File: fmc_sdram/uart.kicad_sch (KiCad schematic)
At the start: 10 parts, among them J2 TYPE-C-31-M-12, U5 TPD4E02B04DQA, U6 CH343P

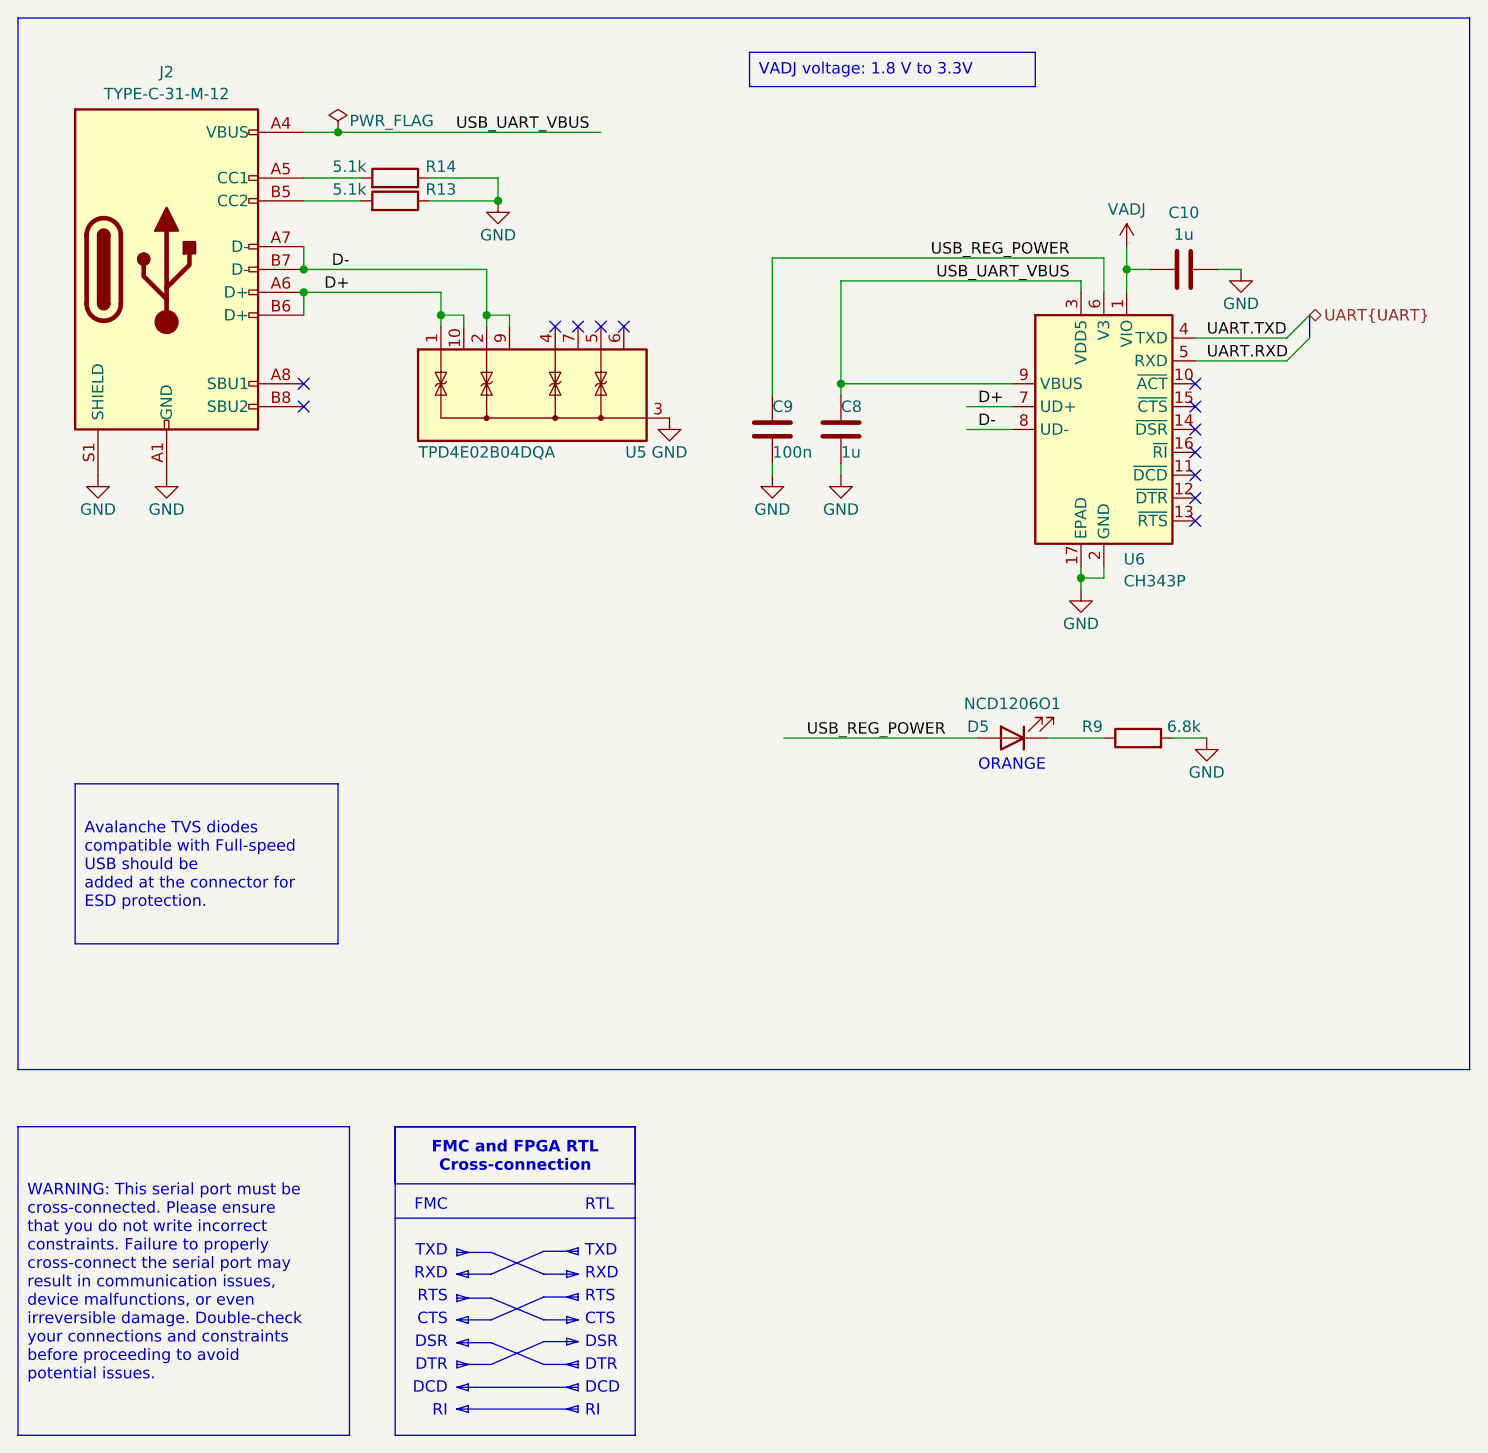
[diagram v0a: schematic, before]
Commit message: fmc_sdram: tie dqm level shifter dir pins to vadj and fix pcb
Signed-off-by: Huang Rui <vowstar@gmail.com>
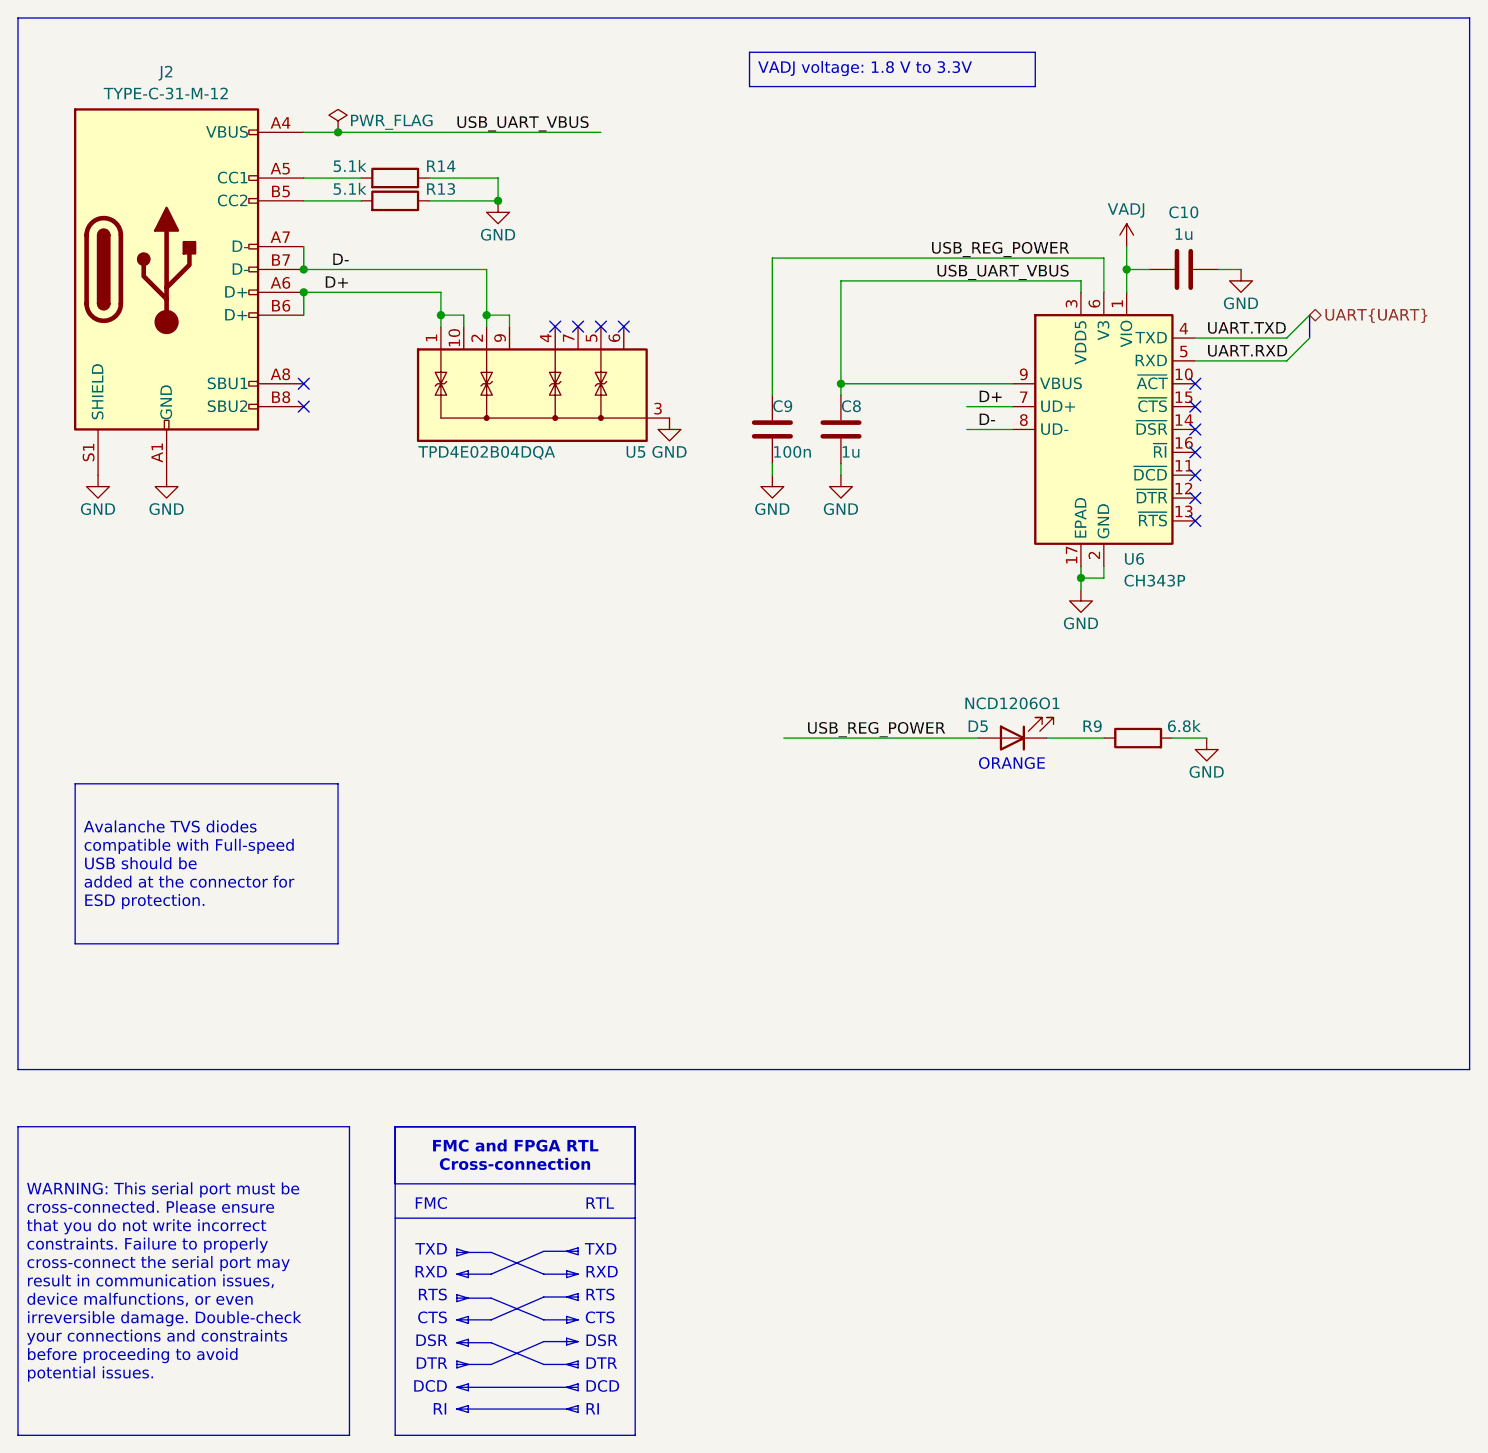
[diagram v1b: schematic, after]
